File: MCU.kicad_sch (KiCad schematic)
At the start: 66 parts, among them J18 Screw_Terminal_01x02, J3 FTSH-107-01-L-D-K, J4 USB_C_Receptacle_USB2.0_16P, Q1 PMOS, SW2 SW_Push, U1 MCP2562-E-SN, U13 TPD2EUSB30, U4 STM32F103C8Tx, U5 AZ1117-3.3, U6 AZ1117-5.0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

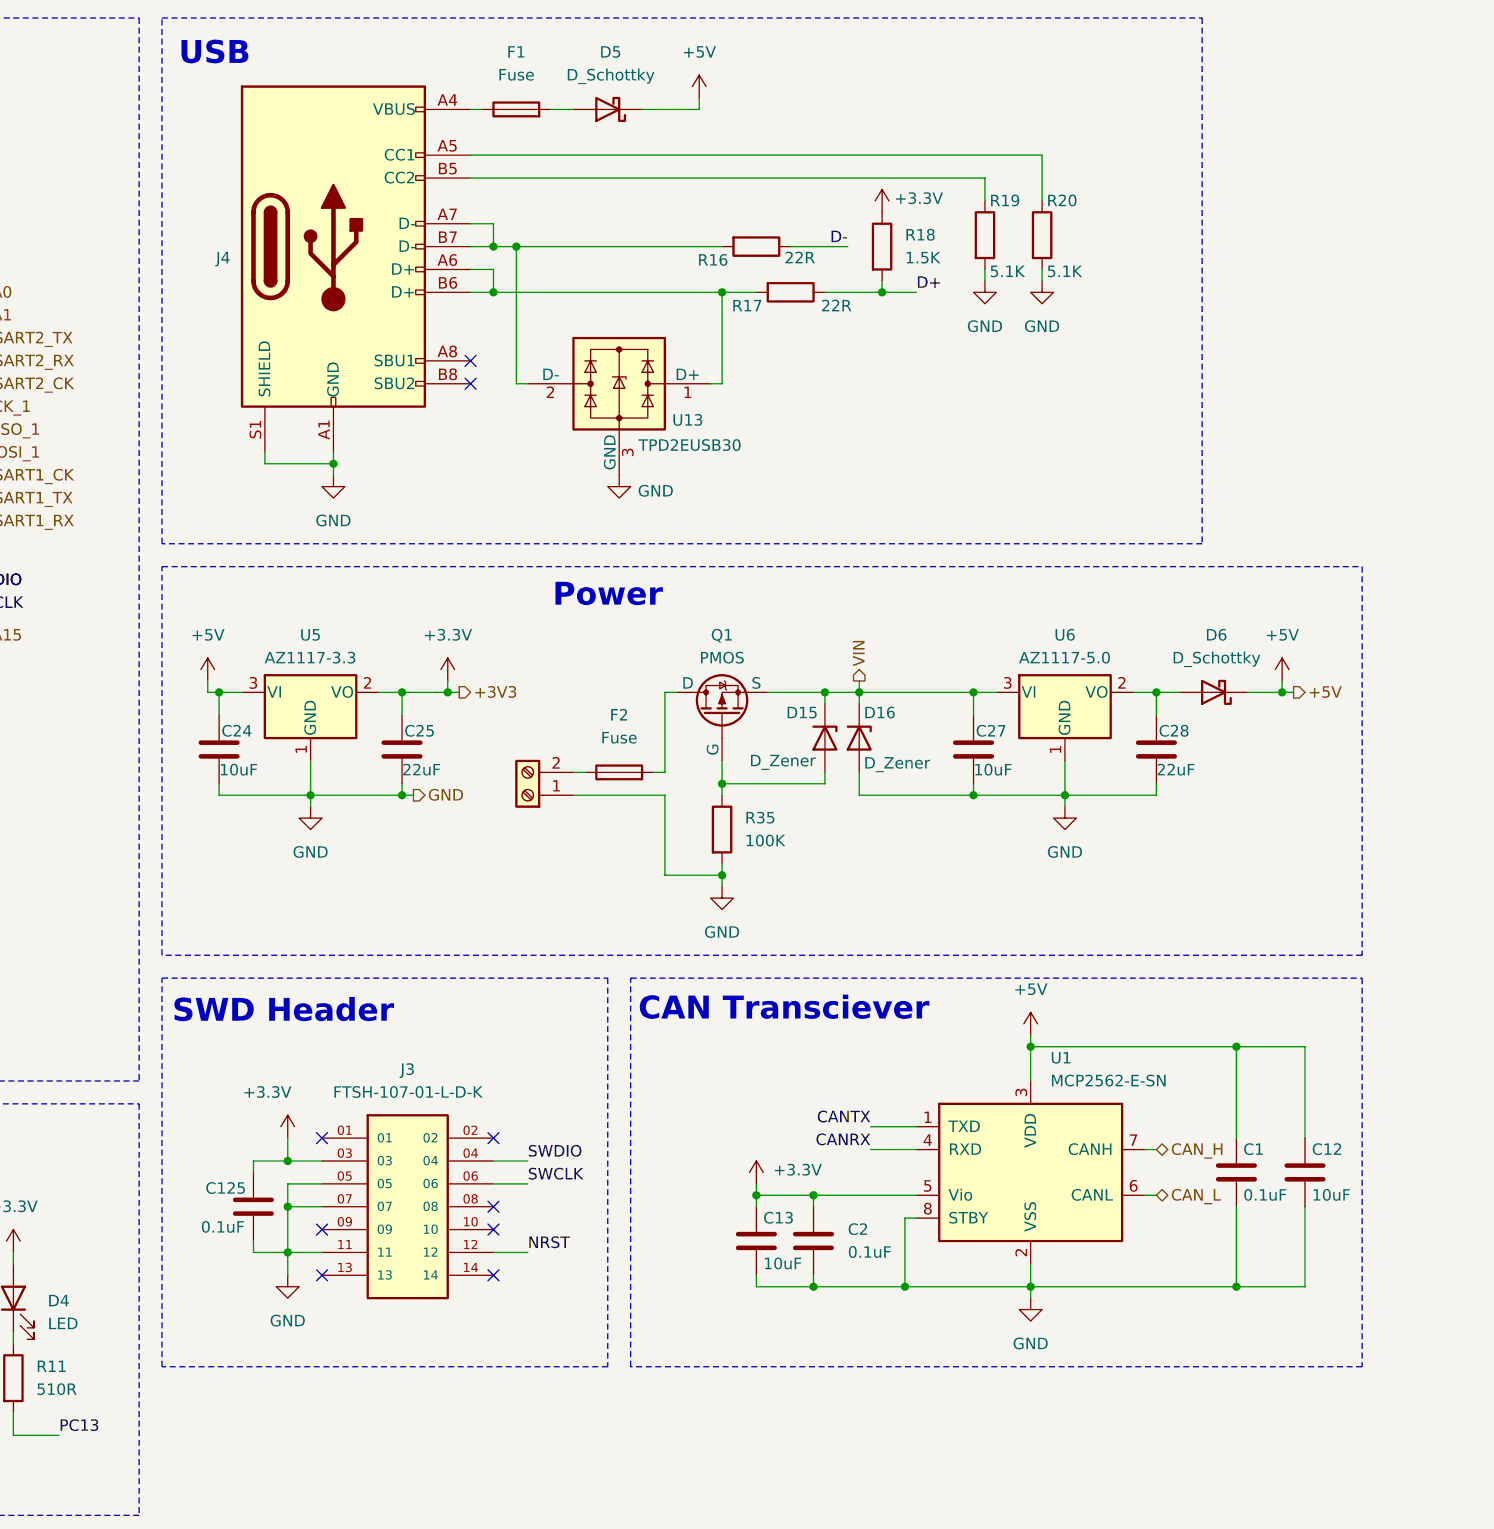
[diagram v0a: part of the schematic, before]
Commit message: Added ideal diodes
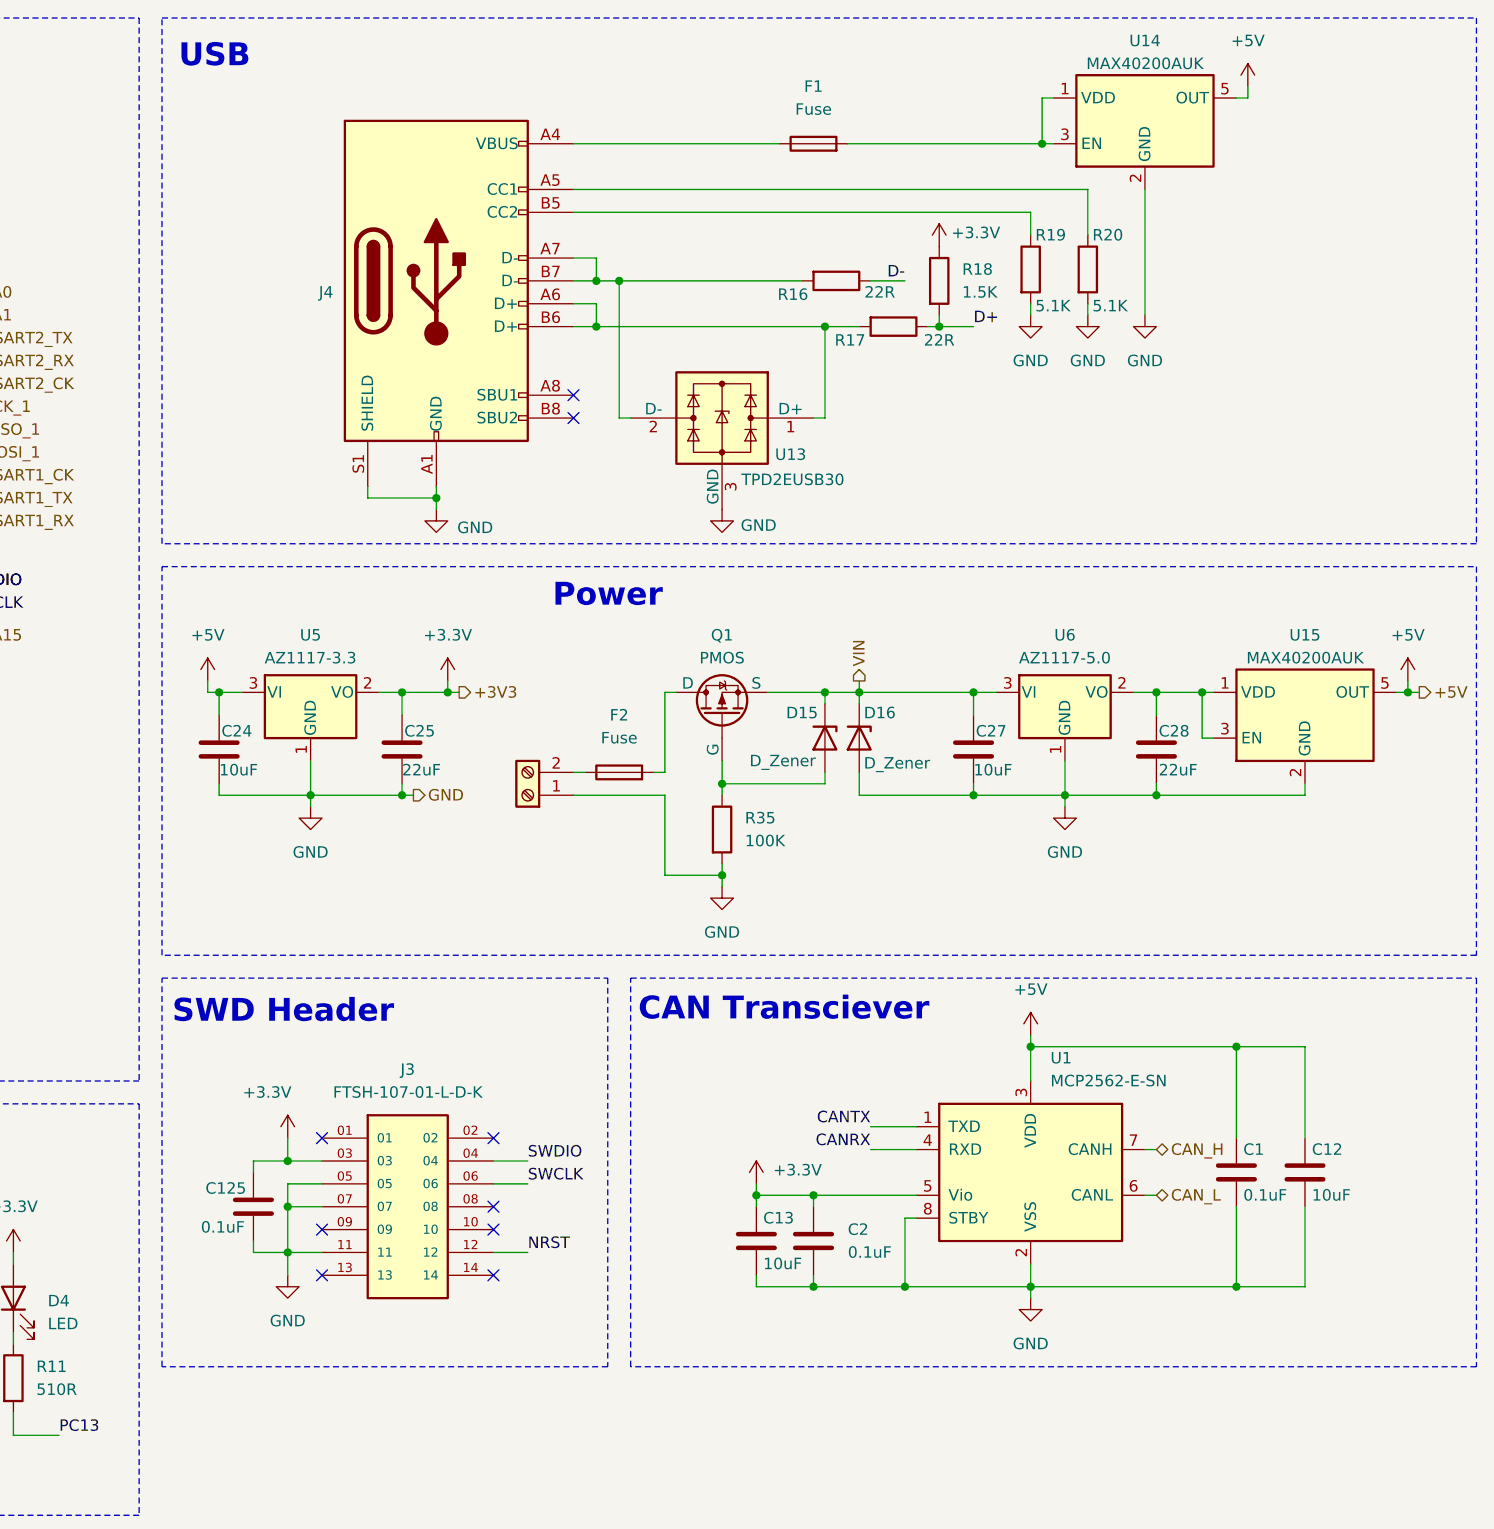
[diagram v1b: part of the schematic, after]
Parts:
- removed D5, D6: D_Schottky, Diode_SMD:D_SOD-123, symbol Device:D_Schottky
- added U14, U15: MAX40200AUK, Package_TO_SOT_SMD:SOT-23-5, symbol Analog_Switch:MAX40200AUK
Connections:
- net +5V: now also U14.5 (OUT), U15.5 (OUT)
- net GND: now also U14.2 (GND), U15.2 (GND)
- net at C28.1, U6.2 (VO): now also U15.1 (VDD), U15.3 (EN)
- net at F1.2: now also U14.1 (VDD), U14.3 (EN)
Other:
- moved on the sheet: F1, J4, R16, R17, R18, R19, R20, U13

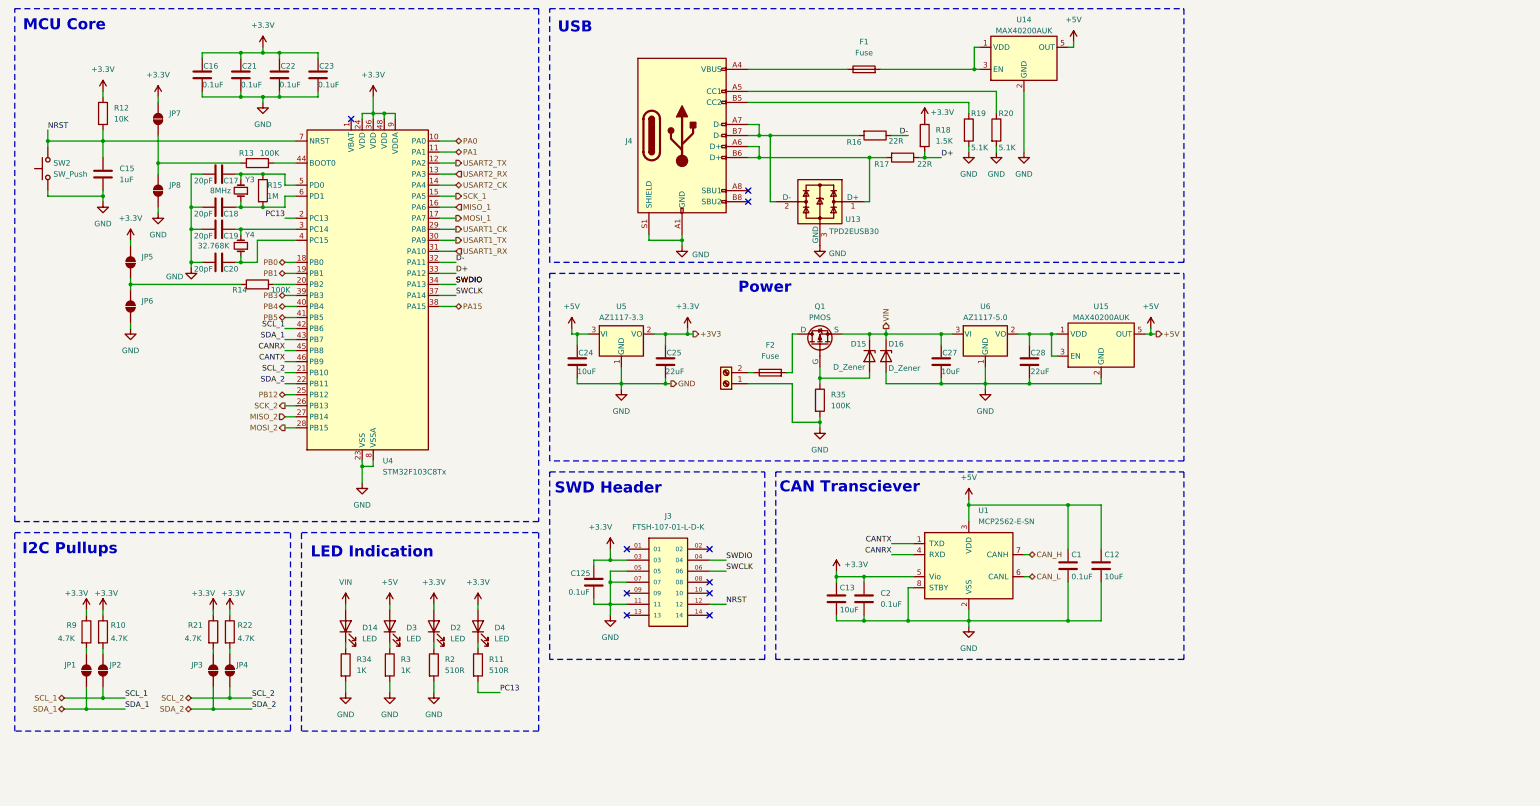
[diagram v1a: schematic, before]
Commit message: Added USB-UART Bridge
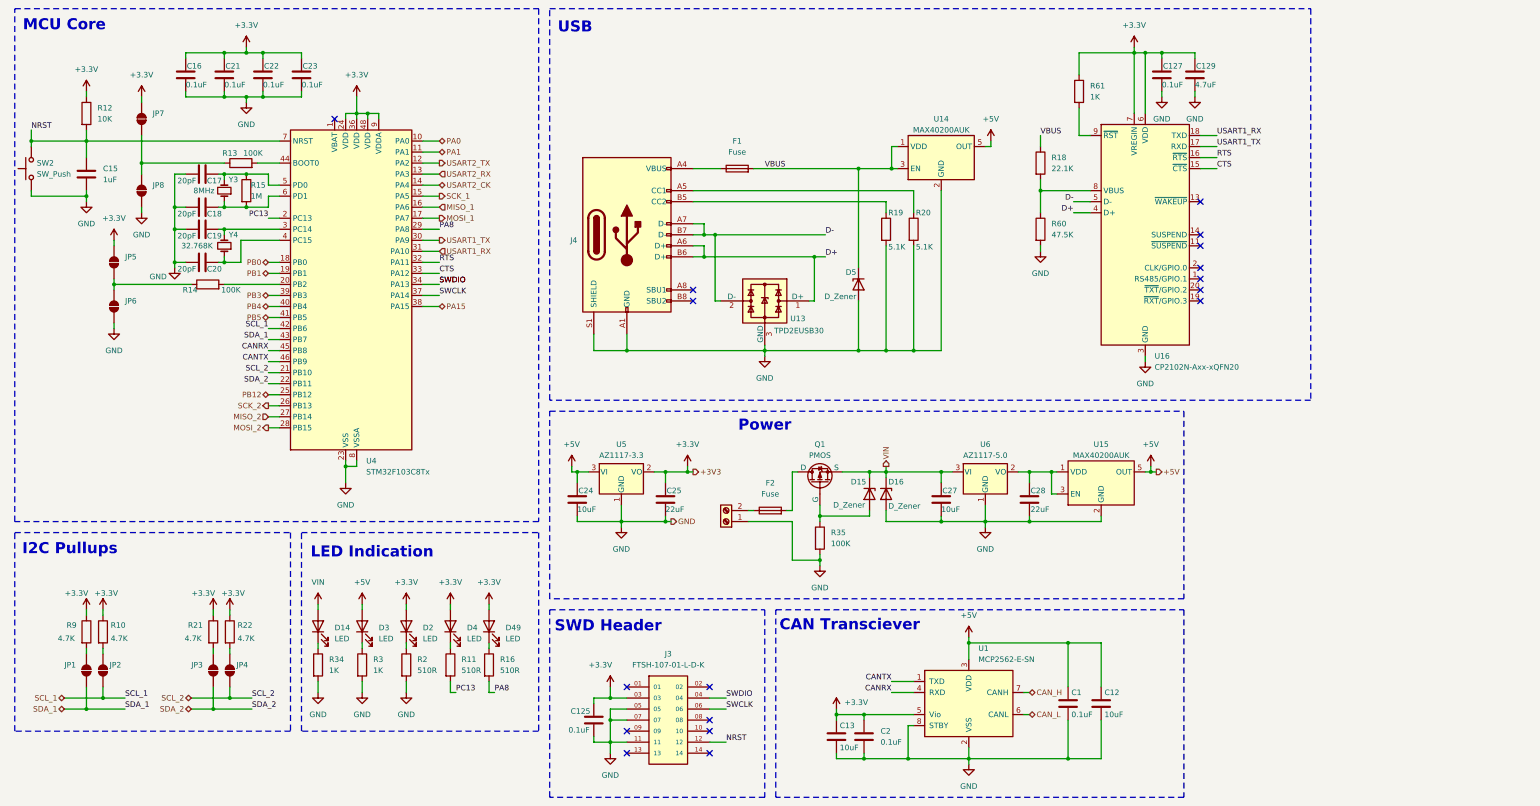
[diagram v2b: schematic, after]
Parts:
- removed R17: 22R, Resistor_SMD:R_0805_2012Metric, symbol Device:R
- added C127: 0.1uF, Capacitor_SMD:C_0805_2012Metric, symbol Device:C
- added C129: 4.7uF, Capacitor_SMD:C_0805_2012Metric, symbol Device:C
- added D49: LED, LED_SMD:LED_0805_2012Metric, symbol Device:LED
- added D5: D_Zener, Diode_SMD:D_SOD-123, symbol Device:D_Zener
- added R60: 47.5K, Resistor_SMD:R_0805_2012Metric, symbol Device:R
- added R61: 1K, Resistor_SMD:R_0805_2012Metric, symbol Device:R
- added U16: CP2102N-Axx-xQFN20, Package_DFN_QFN:SiliconLabs_QFN-20-1EP_3x3mm_P0.5mm_EP1.8x1.8mm, symbol Interface_USB:CP2102N-Axx-xQFN20
- R16: value 22R -> 510R
- R18: value 1.5K -> 22.1K
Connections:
- net +3.3V: now also C127.1, C129.1, D49.2 (A), R61.1, U16.6 (VDD), U16.7 (VREGIN); no longer R18.1
- net D+: now also J4.A6 (D+), J4.B6 (D+), U13.1 (D+), U16.4 (D+); no longer R18.2, U4.33 (PA12)
- net D-: now also J4.A7 (D-), J4.B7 (D-), U13.2 (D-), U16.5 (D-); no longer R16.1, U4.32 (PA11)
- net GND: now also C127.2, C129.2, D5.2 (A), R60.2, U16.12 (GND), U16.21 (GND), U16.3 (GND)
- net USART1_RX: now also U16.18 (TXD)
- net USART1_TX: now also U16.17 (RXD)
- net VBUS: now reaches F1.2, U14.1 (VDD), U14.3 (EN)
- net VBUS: now also R18.1, D5.1 (K)
- net USART1_CK renamed PA8
- net PA8: now also R16.2
- new net: R61.2, U16.9 (~{RST})
- new net: R18.2, R60.1, U16.8 (VBUS)
- new net: D49.1 (K), R16.1
- new net CTS: U16.15 (~{CTS}), U4.33 (PA12)
- new net RTS: U16.16 (~{RTS}), U4.32 (PA11)
- no-connect marks 10 -> 17
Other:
- moved on the sheet: C1, C12, C125, C13, C15, C16, C17, C18, C19, C2, C20, C21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

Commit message: Final updates for R2
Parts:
- removed J18: Screw_Terminal_01x02, TerminalBlock_Phoenix:TerminalBlock_Phoenix_PT-1,5-2-3.5-H_1x02_P3.50mm_Horizontal, symbol Connector:Screw_Terminal_01x02
- added C101, C130: 0.1uF, Capacitor_SMD:C_0805_2012Metric, symbol Device:C
- added C102: 1uF, Capacitor_SMD:C_0805_2012Metric, symbol Device:C
- added C128: 0.22uF, Capacitor_SMD:C_0805_2012Metric, symbol Device:C
- added C131: 4.7uF, Capacitor_SMD:C_0805_2012Metric, symbol Device:C
- added J13: 2068320402, CONN_2068320000-SD_04_MOL, symbol Misc:2068320402
- added Q10: NMOS, Package_TO_SOT_SMD:SOT-23-3, symbol Simulation_SPICE:NMOS
- added R17, R63: 100K, Resistor_SMD:R_0805_2012Metric, symbol Device:R
- added R62: 47K, Resistor_SMD:R_0805_2012Metric, symbol Device:R
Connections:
- net +3.3V: now also C130.1, C131.1
- net +5V: now also C101.1
- net GND: now also C101.2, C102.2, C128.2, C130.2, C131.2, J13.3, J13.4, Q10.3 (S), R63.2
- net VBUS: now also C102.1, R17.2; no longer U14.3 (EN)
- net VIN: now also R62.2
- net at F2.1: now also J13.1, J13.2
- net CTS renamed USART1_RTS
- net RTS renamed USART1_CTS
- new net: Q10.1 (D), R17.1, U14.3 (EN)
- new net: C128.1, Q10.2 (G), R62.1, R63.1
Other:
- moved on the sheet: C127, C129, C24, C25, C27, C28, D15, D16, F2, Q1, R18, R35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

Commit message: libraries
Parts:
- C17, C18: value 20pF -> 27pF
- C19, C20: value 20pF -> 18pF
- D14: value LED -> LED_R
- D15: value D_Zener -> D_GATE
- D16: value D_Zener -> D_VIN
- D2, D4, D49: value LED -> LED_B
- D3: value LED -> LED_G
- D5: value D_Zener -> D_5V
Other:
- moved on the sheet: C101, C102, C128, C24, C25, C27, C28, D15, D16, D49, D5, F1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

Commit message: test
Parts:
- J13: symbol Misc:2068320402 -> Symbols:2068320402
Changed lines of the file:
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@@
 	)
 	(symbol
-		(lib_id "Misc:2068320402")
+		(lib_id "Symbols:2068320402")
 		(at 231.14 124.46 0)
 		(mirror y)

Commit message: library updates
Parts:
- J13: symbol Symbols:2068320402 -> Misc:2068320402
- J3: footprint Connector_Samtec:SAMTEC_FTSH-107-01-L-D-K -> Footprints:SAMTEC_FTSH-107-01-L-D-K; symbol Connector:FTSH-107-01-L-D-K -> Symbols:FTSH-107-01-L-D-K
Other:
- moved on the sheet: C1, C12, C125, C13, C2, J3, U1

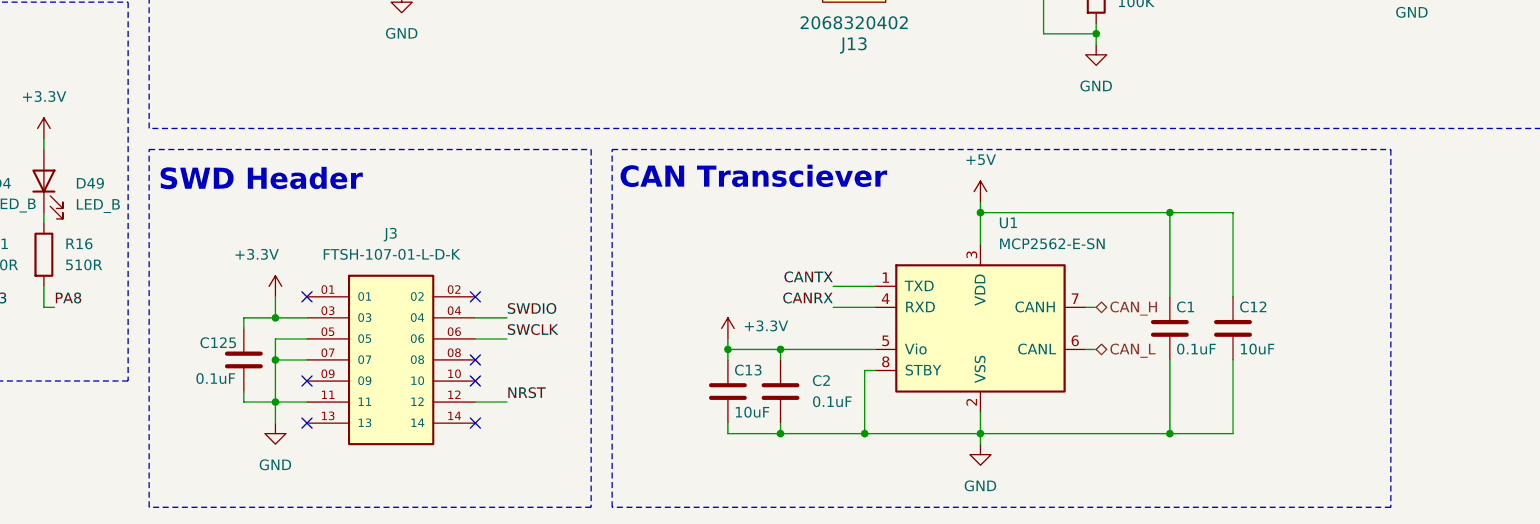
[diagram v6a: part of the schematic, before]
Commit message: Updated libraries
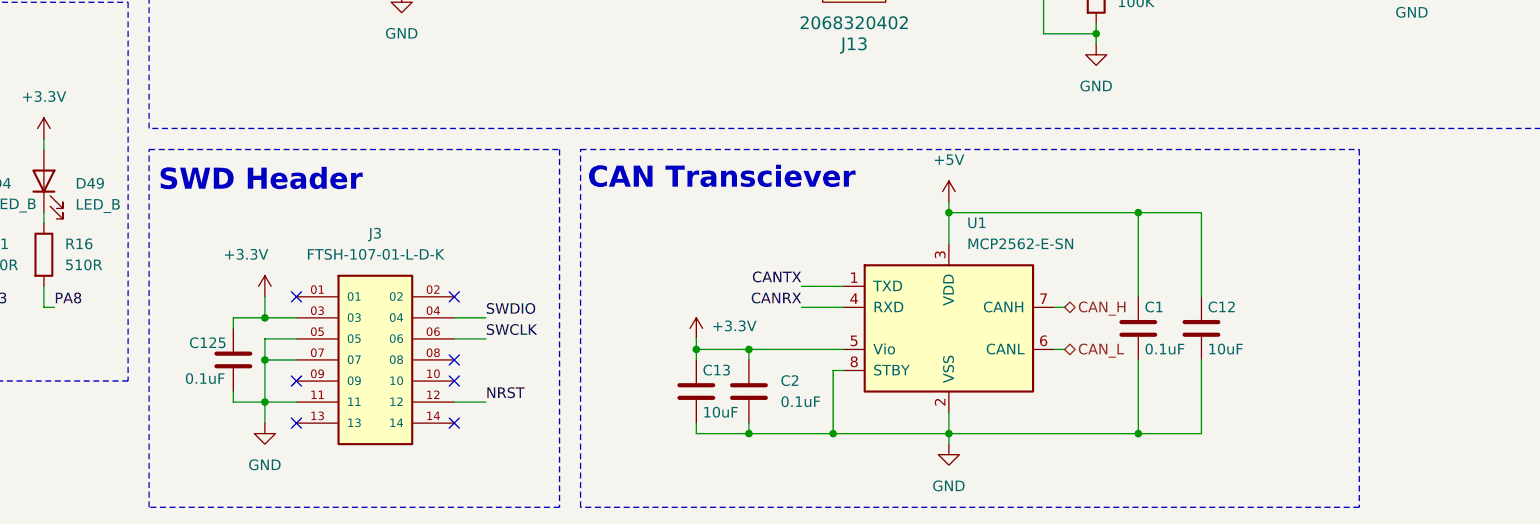
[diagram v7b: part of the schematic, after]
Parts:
- J13: footprint CONN_2068320000-SD_04_MOL -> Footprints:CONN_2068320000-SD_04_MOL; symbol Misc:2068320402 -> Symbols:2068320402
- J3: symbol Symbols:FTSH-107-01-L-D-K -> Connector:FTSH-107-01-L-D-K
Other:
- moved on the sheet: C1, C12, C125, C13, C2, J3, U1
